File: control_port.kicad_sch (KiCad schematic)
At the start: 29 parts, among them IC1 ECP5-BGA256, U16 PI3USB102G, U8 USB3343-CP

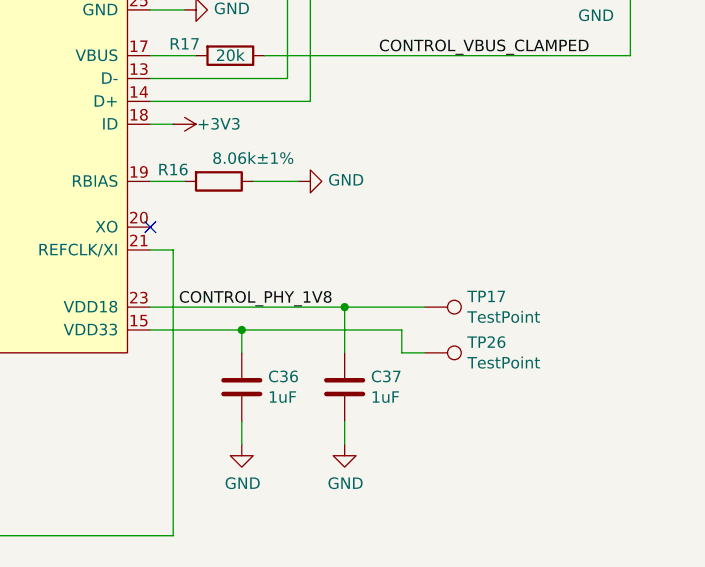
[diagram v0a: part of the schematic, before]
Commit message: Connect PHY pin 15 VDD33 to +3V3
This bypasses the PHY's internal 3.3 V regulator and ties it to the
board's +3V3 net, taking advantage of the superior decoupling of +3V3.
VDD33 test points are retained for test jig compatibility and in case
this change is reverted, but they could be removed in the future.
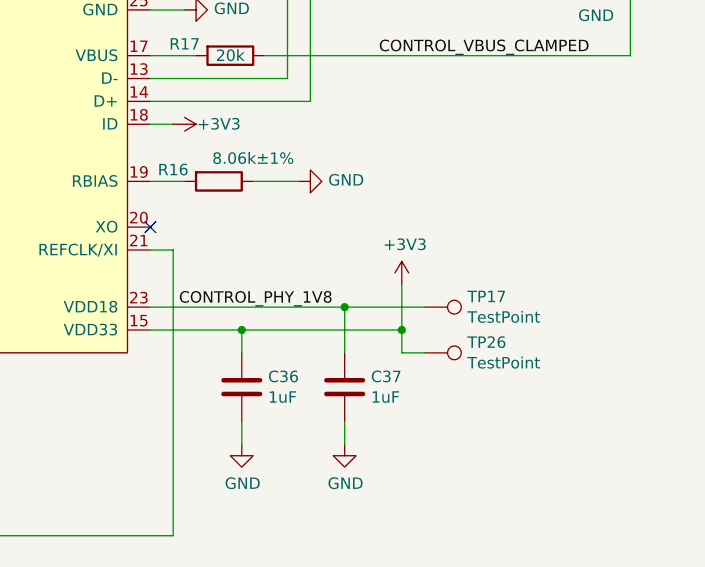
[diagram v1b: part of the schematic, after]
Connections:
- net +3V3: now also C36.1, TP26.1, U8.15 (VDD33)
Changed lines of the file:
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@@
     (comment 1 "Licensed under the CERN-OHL-P v2")
+  )
+  (junction (at 254 127) (diameter 0) (color 0 0 0 0)
   )
   (junction (at 52.07 52.07) (diameter 0) (color 0 0 0 0)
@@
   )
   (wire (pts (xy 232.41 43.815) (xy 200.66 43.815))
+    (stroke (width 0) (type default) (color 0 0 0 0))
+  )
+  (wire (pts (xy 254 121.92) (xy 254 127))
     (stroke (width 0) (type default) (color 0 0 0 0))
   )
@@
       (effects (font (size 1.27 1.27)) hide)
     )
+    (pin "1")
+  )
+  (symbol (lib_id "power:+3V3") (at 254 121.92 0) (unit 1)
+    (in_bom yes) (on_board yes)
+    (property "Reference" "#PWR0235" (id 0) (at 254 125.73 0)
+      (effects (font (size 1.27 1.27)) hide)
+    )
+    (property "Value" "+3V3" (id 1) (at 254.3556 117.5258 0))
+    (property "Footprint" "" (id 2) (at 254 121.92 0)
+      (effects (font (size 1.27 1.27)) hide)
+    )
+    (property "Datasheet" "" (id 3) (at 254 121.92 0)
+      (effects (font (size 1.27 1.27)) hide)
+    )

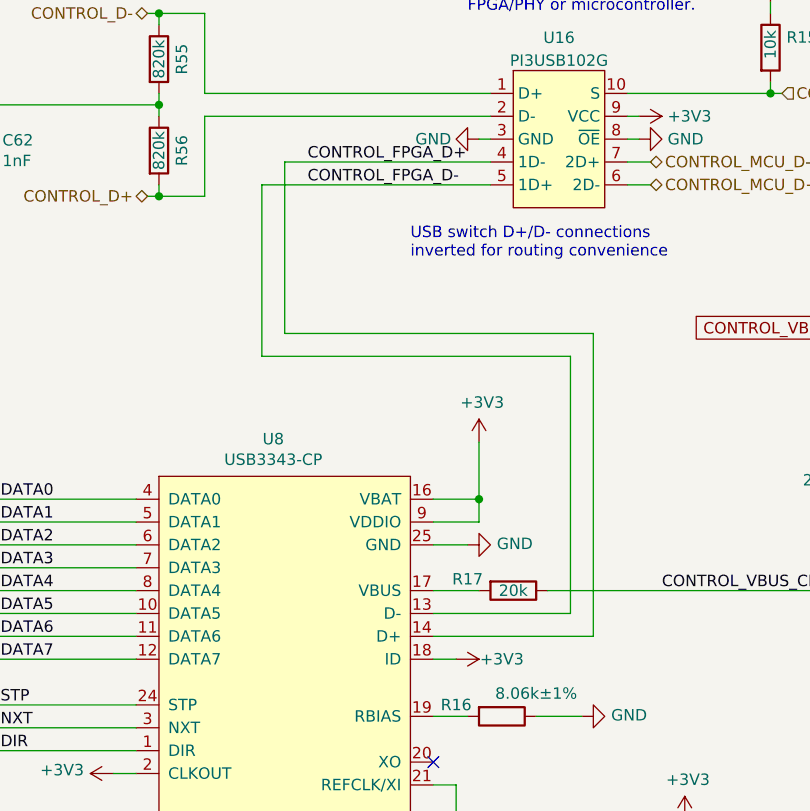
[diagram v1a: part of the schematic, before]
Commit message: Add a common-mode choke to each USB PHY
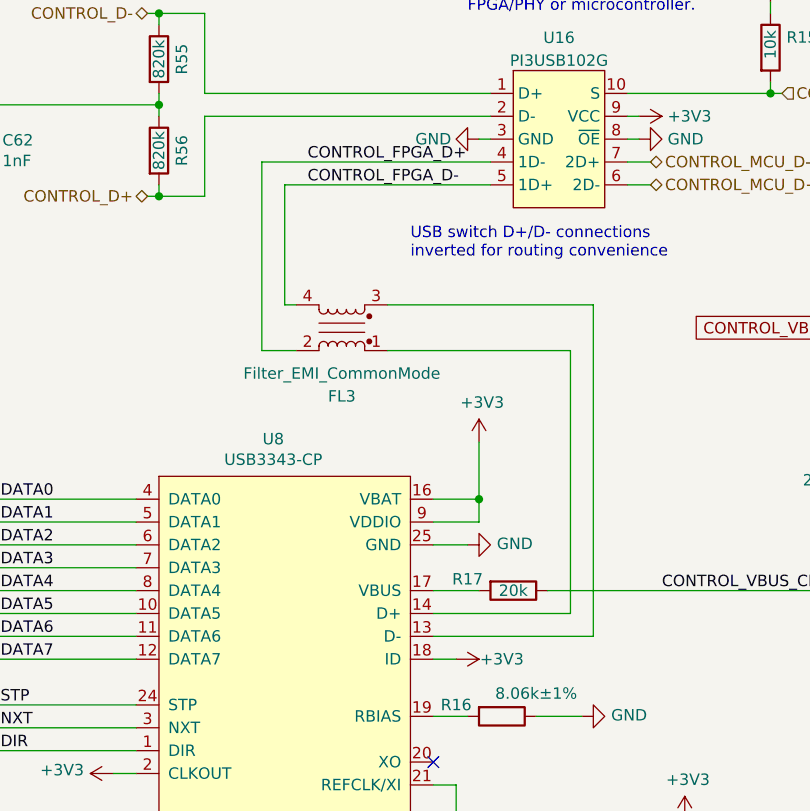
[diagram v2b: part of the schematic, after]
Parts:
- added FL3: Filter_EMI_CommonMode, cynthion:L_CommonModeChoke_Murata_DLM0NS, symbol Device:Filter_EMI_CommonMode
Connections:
- net CONTROL_FPGA_D+: now also FL3.2; no longer U8.14 (D+)
- net CONTROL_FPGA_D-: now also FL3.4; no longer U8.13 (D-)
- new net: FL3.3, U8.13 (D-)
- new net: FL3.1, U8.14 (D+)
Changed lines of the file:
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@@
     (stroke (width 0) (type default) (color 0 0 0 0))
   )
-  (wire (pts (xy 207.01 70.485) (xy 207.01 51.435))
+  (wire (pts (xy 209.55 64.77) (xy 209.55 51.435))
     (stroke (width 0) (type default) (color 0 0 0 0))
   )
@@
     (stroke (width 0) (type default) (color 0 0 0 0))
   )
-  (wire (pts (xy 209.55 48.895) (xy 209.55 67.945))
+  (wire (pts (xy 207.01 48.895) (xy 207.01 69.85))
     (stroke (width 0) (type default) (color 0 0 0 0))
   )
@@
     (stroke (width 0) (type default) (color 0 0 0 0))
   )
-  (wire (pts (xy 241.3 99.06) (xy 241.3 70.485))
-    (stroke (width 0) (type default) (color 0 0 0 0))
-  )
   (wire (pts (xy 193.04 88.9) (xy 156.21 88.9))
     (stroke (width 0) (type default) (color 0 0 0 0))
@@
     (stroke (width 0) (type default) (color 0 0 0 0))
   )
-  (wire (pts (xy 209.55 67.945) (xy 243.84 67.945))
-    (stroke (width 0) (type default) (color 0 0 0 0))
-  )
   (wire (pts (xy 115.57 34.29) (xy 115.57 35.56))
     (stroke (width 0) (type default) (color 0 0 0 0))
@@
     (stroke (width 0) (type default) (color 0 0 0 0))
   )
-  (wire (pts (xy 209.55 48.895) (xy 232.41 48.895))
+  (wire (pts (xy 207.01 48.895) (xy 232.41 48.895))
     (stroke (width 0) (type default) (color 0 0 0 0))
   )
@@
     (stroke (width 0) (type default) (color 0 0 0 0))
   )
+  (wire (pts (xy 220.98 64.77) (xy 243.84 64.77))
+    (stroke (width 0) (type default) (color 0 0 0 0))
+  )
   (wire (pts (xy 228.6 104.14) (xy 226.06 104.14))
     (stroke (width 0) (type default) (color 0 0 0 0))
@@
     (stroke (width 0) (type default) (color 0 0 0 0))
   )
+  (wire (pts (xy 241.3 99.06) (xy 241.3 69.85))
+    (stroke (width 0) (type default) (color 0 0 0 0))
+  )
   (wire (pts (xy 195.58 41.275) (xy 195.58 42.545))
     (stroke (width 0) (type default) (color 0 0 0 0))
@@
     (stroke (width 0) (type default) (color 0 0 0 0))
   )
+  (wire (pts (xy 209.55 64.77) (xy 210.82 64.77))
+    (stroke (width 0) (type default) (color 0 0 0 0))
+  )
+  (wire (pts (xy 241.3 69.85) (xy 220.98 69.85))
+    (stroke (width 0) (type default) (color 0 0 0 0))
+  )
   (wire (pts (xy 110.49 99.06) (xy 110.49 91.44))
     (stroke (width 0) (type default) (color 0 0 0 0))
@@
     (stroke (width 0) (type default) (color 0 0 0 0))
   )
+  (wire (pts (xy 243.84 64.77) (xy 243.84 101.6))
+    (stroke (width 0) (type default) (color 0 0 0 0))
+  )
   (wire (pts (xy 124.46 127) (xy 123.19 127))
     (stroke (width 0) (type default) (color 0 0 0 0))
@@
     (stroke (width 0) (type default) (color 0 0 0 0))
   )
+  (wire (pts (xy 210.82 69.85) (xy 207.01 69.85))
+    (stroke (width 0) (type default) (color 0 0 0 0))
+  )
   (wire (pts (xy 46.99 49.53) (xy 46.99 52.07))
     (stroke (width 0) (type default) (color 0 0 0 0))
@@
     (stroke (width 0) (type default) (color 0 0 0 0))
   )
-  (wire (pts (xy 207.01 51.435) (xy 232.41 51.435))
+  (wire (pts (xy 209.55 51.435) (xy 232.41 51.435))
     (stroke (width 0) (type default) (color 0 0 0 0))
   )
@@
     (stroke (width 0) (type default) (color 0 0 0 0))
   )
-  (wire (pts (xy 241.3 70.485) (xy 207.01 70.485))
-    (stroke (width 0) (type default) (color 0 0 0 0))
-  )
   (wire (pts (xy 63.5 41.91) (xy 63.5 34.29))
     (stroke (width 0) (type default) (color 0 0 0 0))
@@
   )
   (wire (pts (xy 242.57 110.49) (xy 237.49 110.49))
-    (stroke (width 0) (type default) (color 0 0 0 0))
-  )
-  (wire (pts (xy 243.84 67.945) (xy 243.84 101.6))
     (stroke (width 0) (type default) (color 0 0 0 0))
   )
@@
     (pin "2")
   )
+  (symbol (lib_id "Device:Filter_EMI_CommonMode") (at 215.9 67.31 180) (unit 1)
+    (in_bom yes) (on_board yes)
+    (property "Reference" "FL3" (id 0) (at 215.9 74.93 0))
+    (property "Value" "Filter_EMI_CommonMode" (id 1) (at 215.9 72.3931 0))
+    (property "Footprint" "cynthion:L_CommonModeChoke_Murata_DLM0NS" (id 2) (at 215.9 68.326 0)
+      (effects (font (size 1.27 1.27)) hide)
+    )
+    (property "Datasheet" "https://www.murata.com/en-global/products/productdata/8799424610334/EFLD0009.pdf" (id 3) (at 215.9 68.326 0)
+      (effects (font (size 1.27 1.27)) hide)
+    )
+    (property "Description" "CMC 100MA 2LN 90 OHM SMD" (id 4) (at 215.9 67.31 0)
+      (effects (font (size 1.27 1.27)) hide)
+    )
+    (property "Manufacturer" "Murata" (id 5) (at 215.9 67.31 0)
+      (effects (font (size 1.27 1.27)) hide)
+    )
+    (property "Part Number" "DLM0NSN900HY2D" (id 6) (at 215.9 67.31 0)
+      (effects (font (size 1.27 1.27)) hide)
+    )
+    (pin "1")
+    (pin "2")
+    (pin "3")
+    (pin "4")
+  )
   (symbol (lib_id "power:GND") (at 231.14 46.355 270) (unit 1)

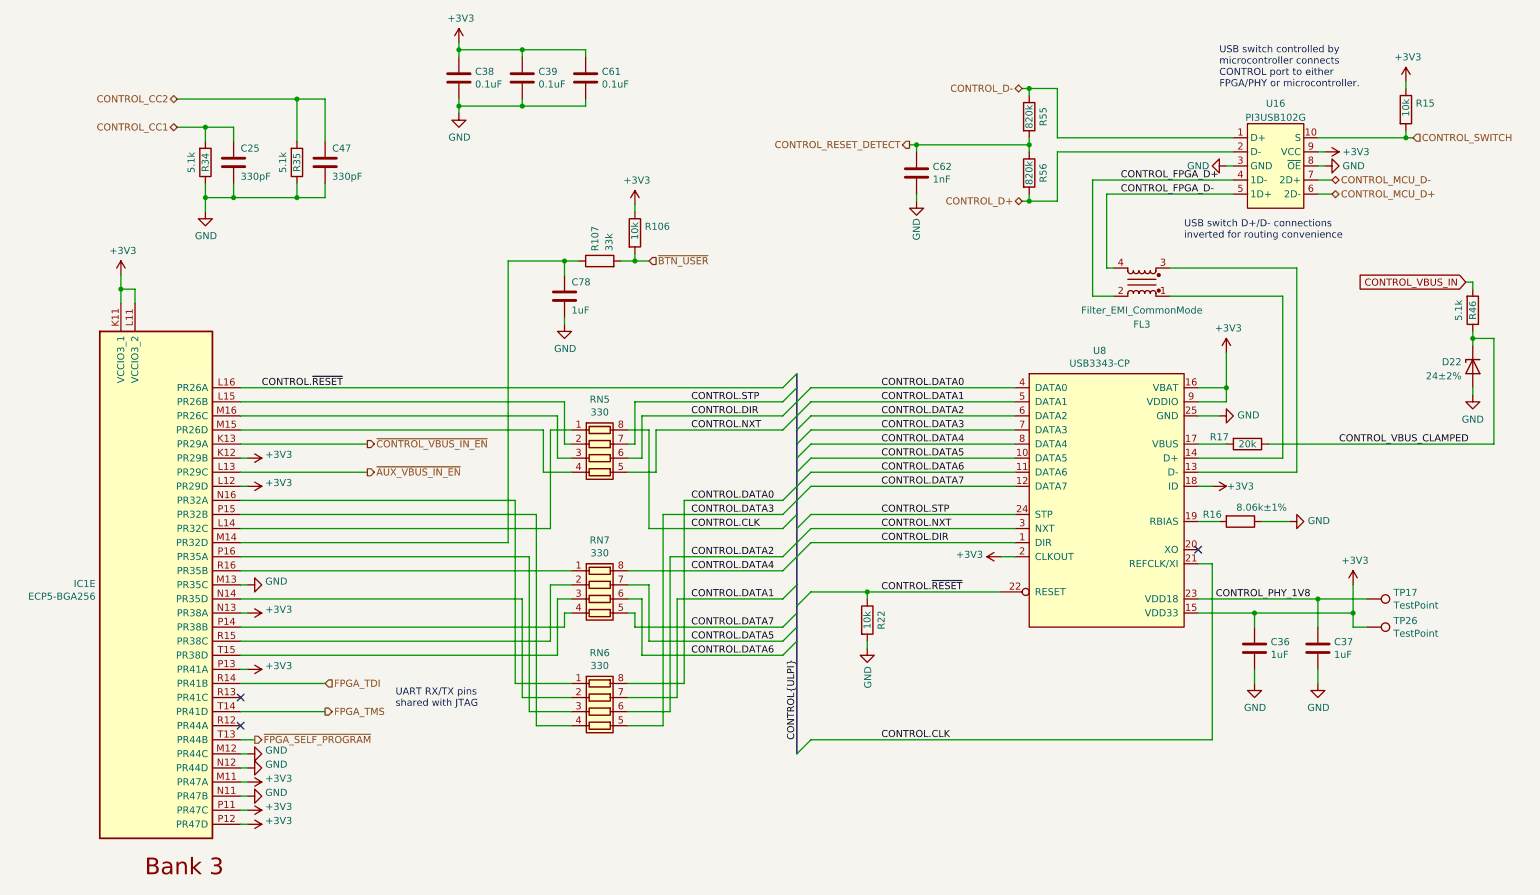
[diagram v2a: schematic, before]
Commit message: Rearrange schematic for readability
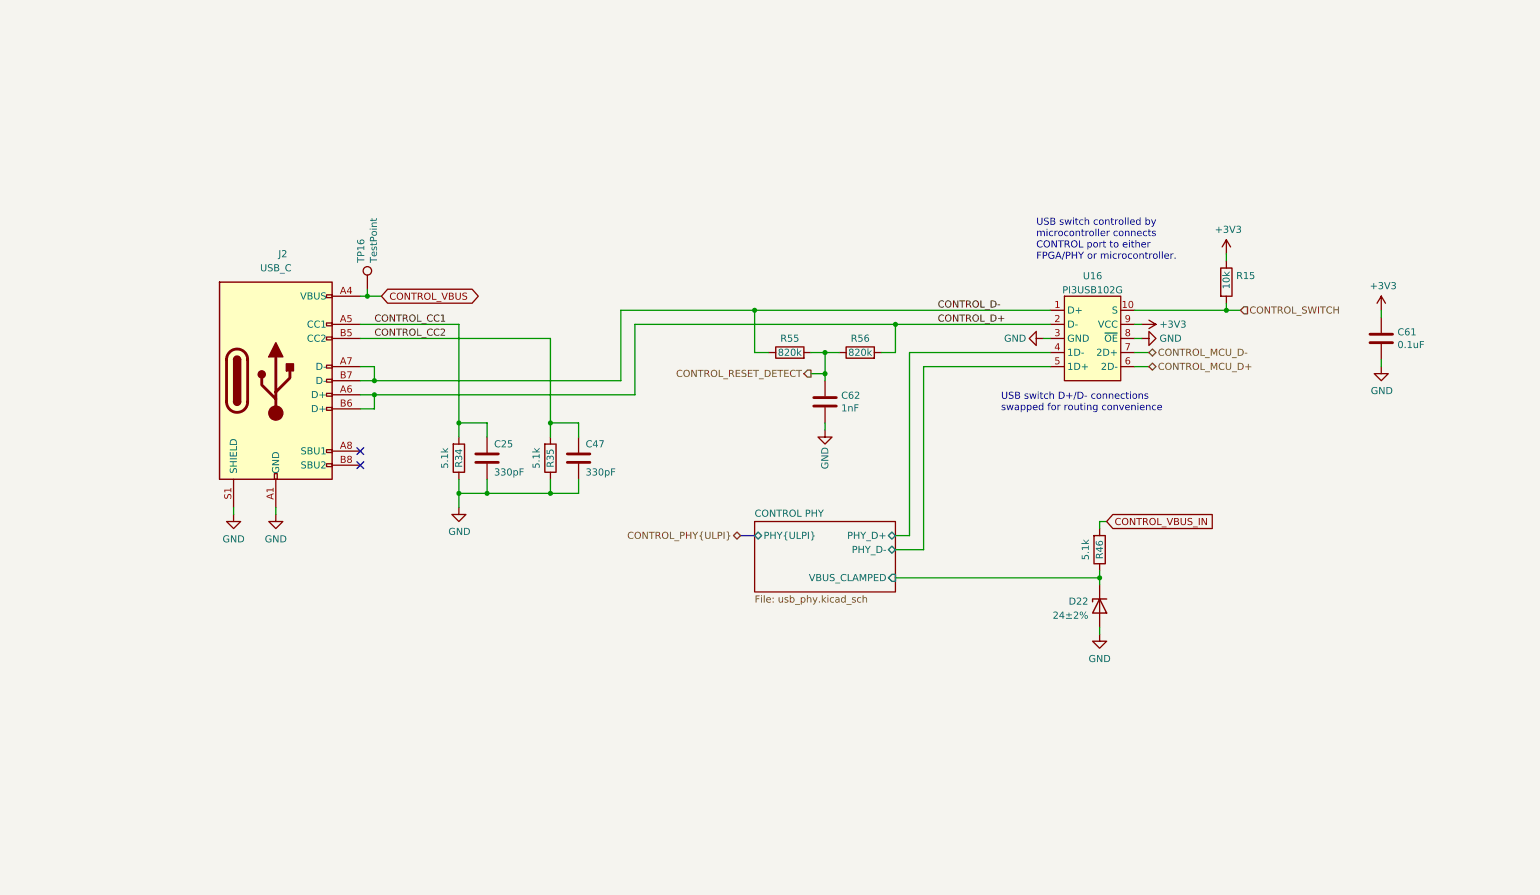
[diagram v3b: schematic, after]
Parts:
- removed C36, C37, C78: 1uF, Capacitor_SMD:C_0402_1005Metric, symbol Device:C
- removed C38, C39: 0.1uF, Capacitor_SMD:C_0402_1005Metric, symbol Device:C
- removed FL3: Filter_EMI_CommonMode, cynthion:L_CommonModeChoke_Murata_DLM0NS, symbol Device:Filter_EMI_CommonMode
- removed IC1: ECP5-BGA256, cynthion:lattice_cabga256, symbol fpgas_and_processors:ECP5-BGA256
- removed R106, R22: 10k, Resistor_SMD:R_0402_1005Metric, symbol Device:R
- removed R107: 33k, Resistor_SMD:R_0402_1005Metric, symbol Device:R
- removed R16: 8.06k±1%, Resistor_SMD:R_0402_1005Metric, symbol Device:R
- removed R17: 20k, Resistor_SMD:R_0402_1005Metric, symbol Device:R
- removed RN5, RN6, RN7: 330, Resistor_SMD:R_Array_Convex_4x0402, symbol Device:R_Pack04
- removed TP17, TP26: TestPoint, TestPoint:TestPoint_Pad_D1.0mm, symbol Connector:TestPoint
- removed U8: USB3343-CP, Package_DFN_QFN:VQFN-24-1EP_4x4mm_P0.5mm_EP2.45x2.45mm, symbol usb:USB3343
- added J2: USB_C, cynthion:USB_C_Receptacle_HRO_TYPE-C-31-M-12, symbol Connector:USB_C_Receptacle_USB2.0
- added TP16: TestPoint, TestPoint:TestPoint_Pad_D1.0mm, symbol Connector:TestPoint
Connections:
- net CONTROL_CC1: now also J2.A5 (CC1)
- net CONTROL_CC2: now also J2.B5 (CC2)
- net CONTROL_D+: now also J2.A6 (D+), J2.B6 (D+)
- net CONTROL_D-: now also J2.A7 (D-), J2.B7 (D-)
- net GND: now also J2.A1 (GND), J2.A12 (GND), J2.B1 (GND), J2.B12 (GND), J2.S1 (SHIELD)
- net CONTROL_FPGA_D+ renamed CONTROL PHY/PHY_D+
- net CONTROL_FPGA_D- renamed CONTROL PHY/PHY_D-
- net CONTROL_VBUS_CLAMPED renamed CONTROL PHY/VBUS_CLAMPED
- new net CONTROL_VBUS: J2.A4 (VBUS), J2.A9 (VBUS), J2.B4 (VBUS), J2.B9 (VBUS), TP16.1
- no-connect marks 3 -> 2
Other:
- added sheet CONTROL PHY (usb_phy.kicad_sch)
- note added: "USB switch D+/D- connections swapped for routing convenience"
- note removed: "UART RX/TX pins shared with JTAG"
- note removed: "USB switch D+/D- connections inverted for routing convenience"
- moved on the sheet: C25, C47, C61, C62, D22, R15, R34, R35, R46, R55, R56, U16

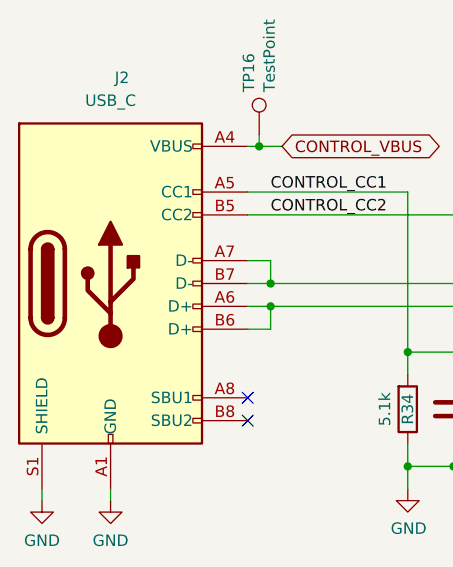
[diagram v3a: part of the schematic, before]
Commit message: Upgrade to KiCad 7
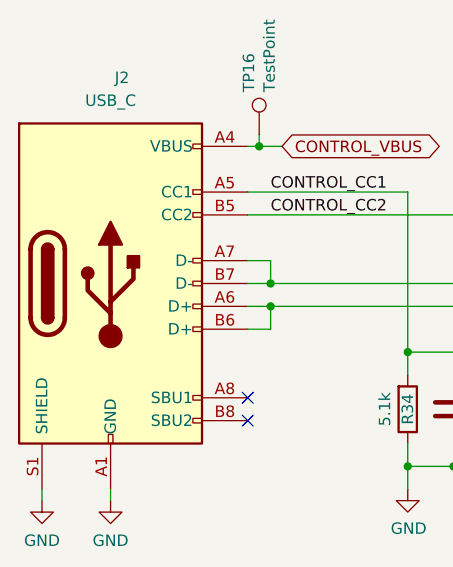
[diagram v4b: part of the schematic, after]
